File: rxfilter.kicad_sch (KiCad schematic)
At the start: 14 parts

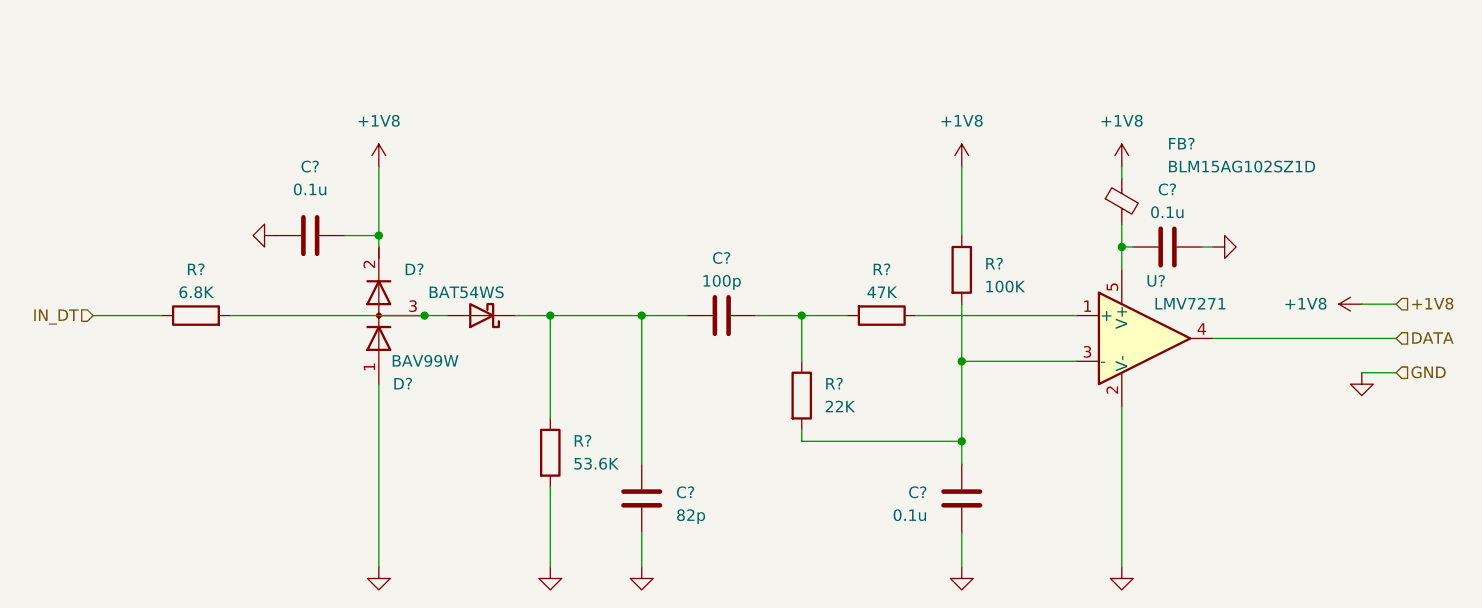
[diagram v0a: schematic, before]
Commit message: G2 revision
G2 revision = Kampela development kit

Features:
- electronics is more stable and reliable
- better power harvesting efficiency
- fixed a touchscreen instability with powerful NFC transmitters
- mechanical layout improved for low-volume productions for a devkit batch
- NFC coil placed closer to the phone antenna. The coil parameters are optimized based on a mathematical model of the NFS harvester circuit.
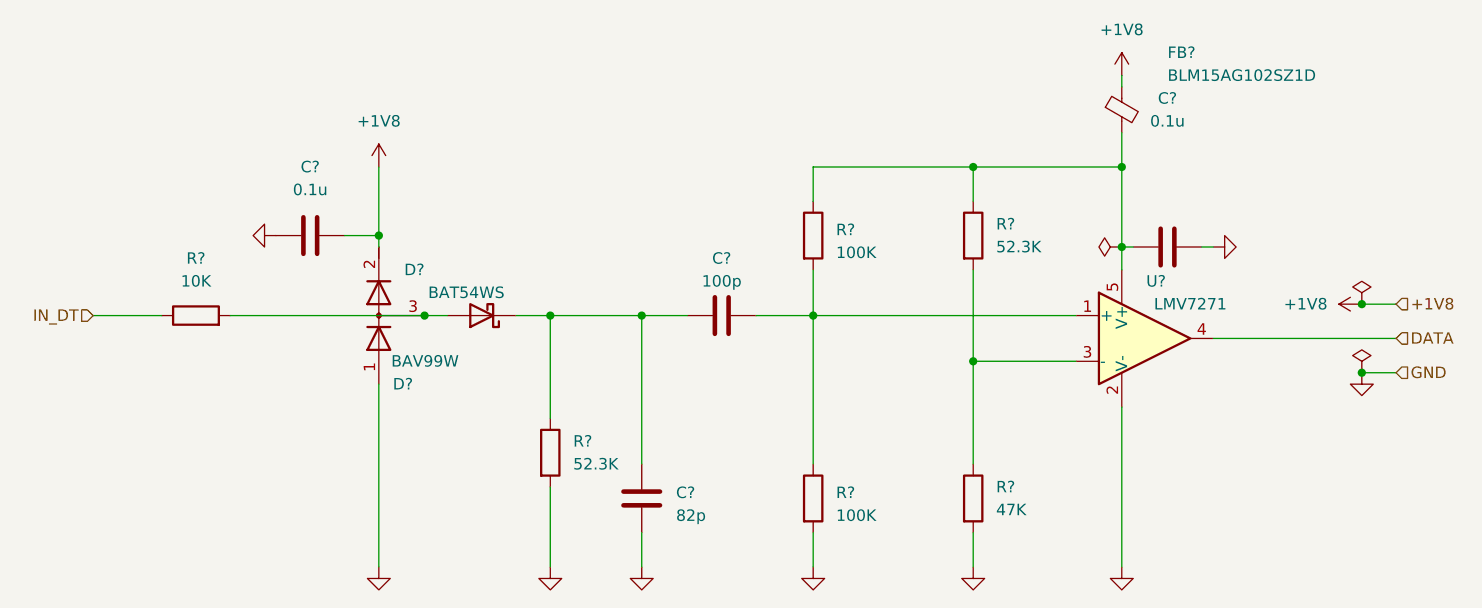
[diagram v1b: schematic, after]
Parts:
- removed C?: 0.1u, Capacitor_SMD:C_0402_1005Metric, symbol Device:C
- removed R?: 47K, Resistor_SMD:R_0402_1005Metric, symbol Device:R
- removed R?: 22K, Resistor_SMD:R_0402_1005Metric, symbol Device:R
- added R?: 47K, Resistor_SMD:R_0402_1005Metric, symbol Device:R
- added R?: 52.3K, Resistor_SMD:R_0402_1005Metric, symbol Device:R
- added R?: 100K, Resistor_SMD:R_0402_1005Metric, symbol Device:R
- R?: value 6.8K -> 10K
- R?: value 53.6K -> 52.3K
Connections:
- net +1V8: no longer R?.1
- net GND: now also R?.2, R?.2
- net at C?.2, FB?.2, U?.5 (V+): now also R?.1, R?.1
- net at U?.1 (+): now also C?.1, R?.2, R?.1
- net at U?.3 (-): now also R?.1, R?.2; no longer R?.2
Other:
- moved on the sheet: FB?, R?

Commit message: G5 revision
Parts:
- removed C?: 0.1u, Capacitor_SMD:C_0402_1005Metric, symbol Device:C
- removed D?: BAV99W, Package_TO_SOT_SMD:SOT-323_SC-70, symbol Device:D_Dual_Series_AKC
- added TP?: TestPoint, TestPoint:TestPoint_Pad_D1.0mm, symbol Connector:TestPoint
- C?: value 82p -> 100p
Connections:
- net DATA: now also TP?.1
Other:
- moved on the sheet: R?

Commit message: Next revision
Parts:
- removed C?: 0.1u, Capacitor_SMD:C_0402_1005Metric, symbol Device:C
- removed C? (x2): 100p, Capacitor_SMD:C_0402_1005Metric, symbol Device:C
- removed FB?: BLM15AG102SZ1D, Inductor_SMD:L_0402_1005Metric, symbol Device:FerriteBead_Small
- removed R?: 47K, Resistor_SMD:R_0402_1005Metric, symbol Device:R
- removed R?: 10K, Resistor_SMD:R_0402_1005Metric, symbol Device:R
- removed R? (x2): 52.3K, Resistor_SMD:R_0402_1005Metric, symbol Device:R
- removed R? (x2): 100K, Resistor_SMD:R_0402_1005Metric, symbol Device:R
- added C1, C2: 100p, Capacitor_SMD:C_0201_0603Metric, symbol Device:C
- added C3: 0.1, Capacitor_SMD:C_0201_0603Metric, symbol Device:C
- added R1: 10K, Resistor_SMD:R_0201_0603Metric, symbol Device:R
- added R2, R5: 52.3K, Resistor_SMD:R_0201_0603Metric, symbol Device:R
- added R3, R4: 100K, Resistor_SMD:R_0201_0603Metric, symbol Device:R
- added R6: 46.4K, Resistor_SMD:R_0201_0603Metric, symbol Device:R
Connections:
- net +1V8: now also U?.5 (V+), C3.1, R3.2, R5.2
- net GND: now also C1.1, C3.2, R2.1, R4.1, R6.1
- net IN_DT: now also R1.1
- net at D?.1 (K): now also C1.2, C2.2, R2.2
- net at D?.2 (A): now also R1.2
- net at U?.1 (+): now also C2.1, R3.1, R4.2
- net at U?.3 (-): now also R5.1, R6.2
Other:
- moved on the sheet: D?
